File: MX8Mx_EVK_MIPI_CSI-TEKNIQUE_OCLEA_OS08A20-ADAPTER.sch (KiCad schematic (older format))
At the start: 11 parts, among them J1 1888863-4, J2 XF2M-3215-1A, U1 NLSX5014DTR2G, U2 SN74LVC1G14DRL

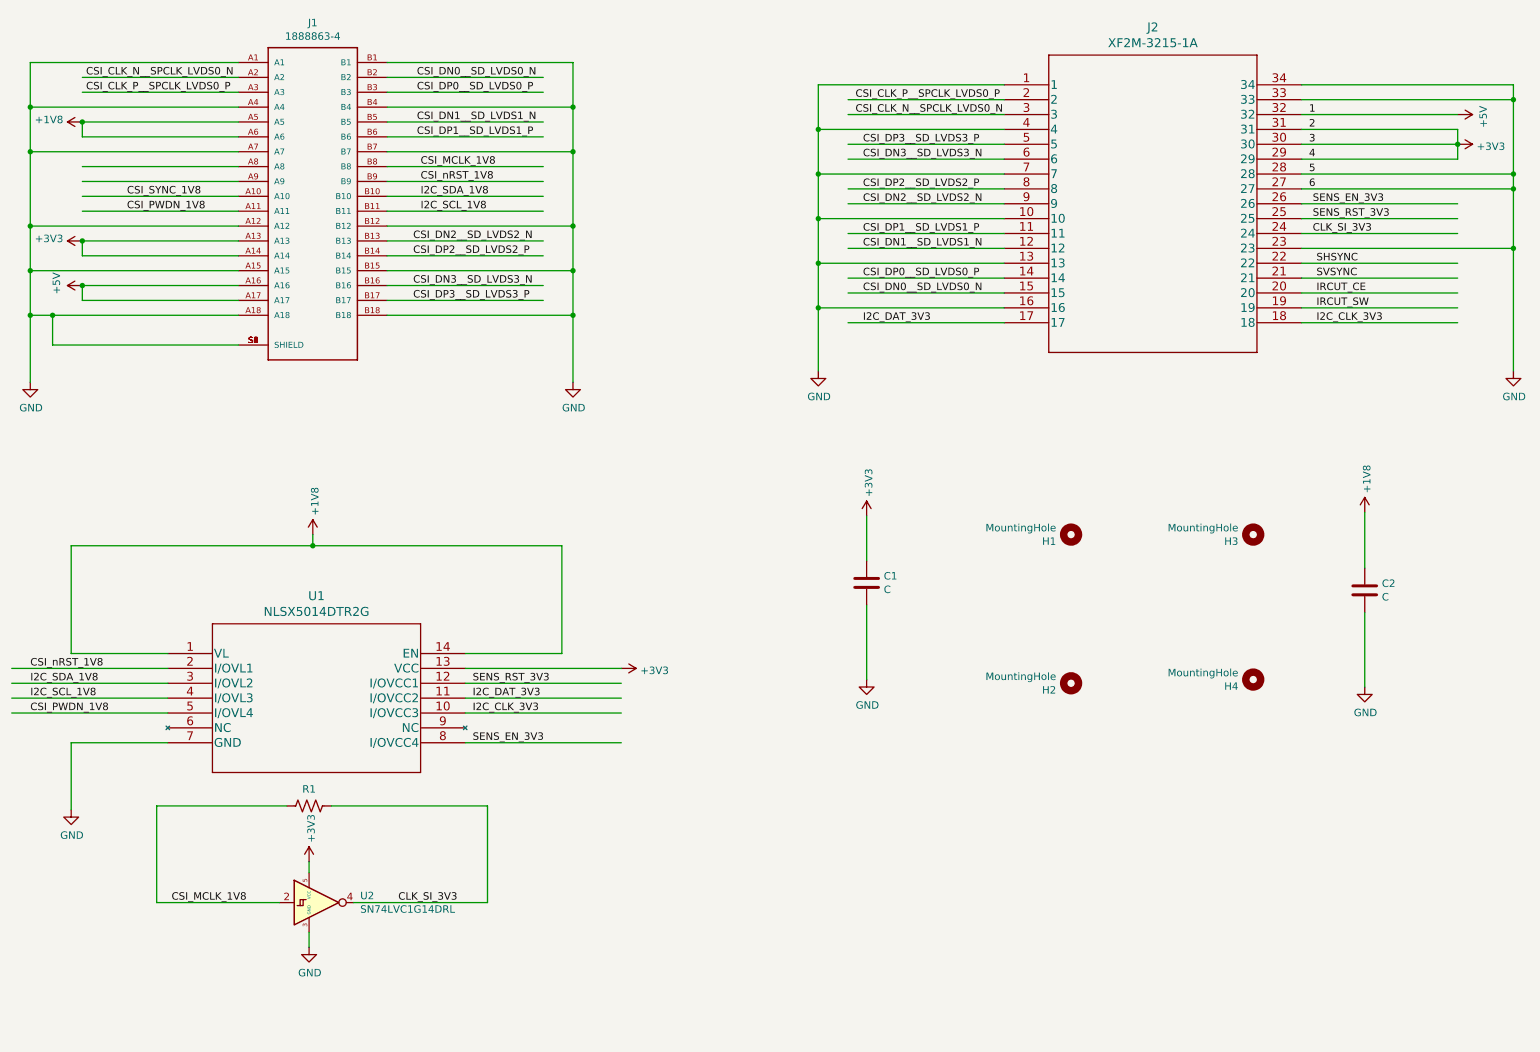
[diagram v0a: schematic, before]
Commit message: Mirror J1 signals (A-side to B-side and vice-versa) for mating with the MIPI-CSI interface(s) on EVK
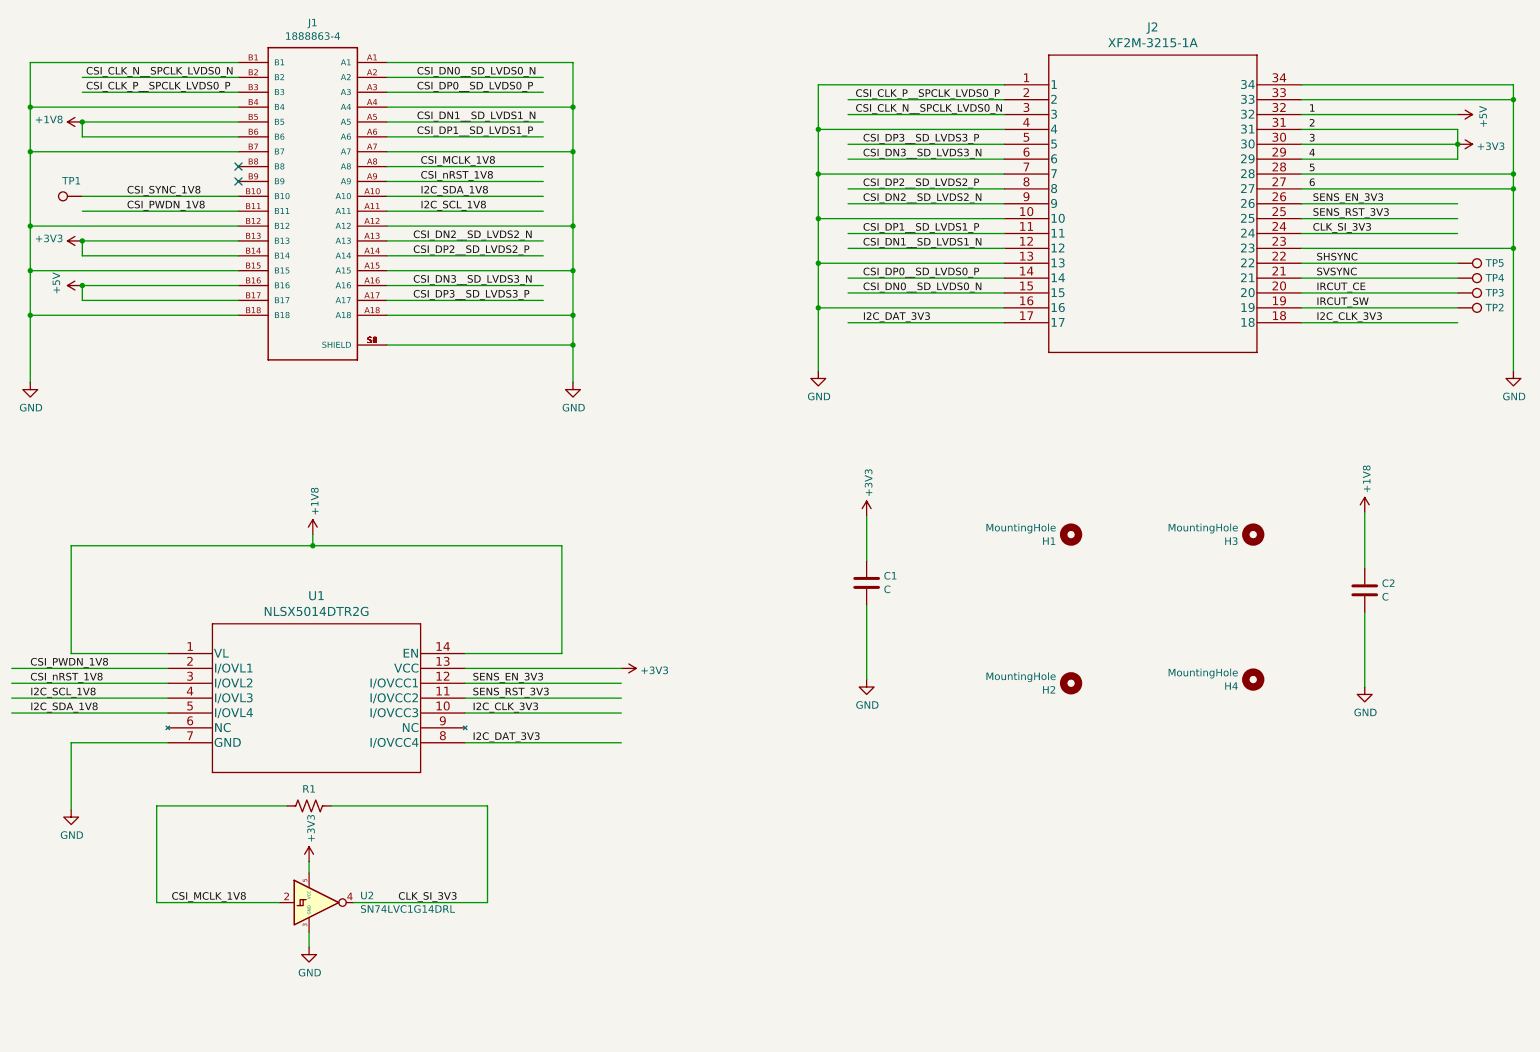
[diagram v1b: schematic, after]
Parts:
- added TP1, TP2, TP3, TP4, TP5: TestPoint, TestPoint:TestPoint_Pad_D1.0mm, symbol Connector:TestPoint
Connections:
- wire segments 131 -> 128
- no-connect marks 0 -> 2
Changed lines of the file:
@@
 	4300 1175 3250 1175
-Wire Wire Line
-	4300 1275 3250 1275
 Wire Wire Line
 	4300 1475 3250 1475
@@
 Text Label 3450 1175 0    50   ~ 0
 CSI_DN0__SD_LVDS0_N
-Text Label 3450 1275 0    50   ~ 0
-CSI_DP0__SD_LVDS0_P
 Text Label 3450 1475 0    50   ~ 0
 CSI_DN1__SD_LVDS1_N
@@
 	2750 4325 4425 4325
 Wire Wire Line
+	1775 5450 725  5450
+Wire Wire Line
+	1775 5350 725  5350
+Wire Wire Line
+	1775 5150 725  5150
+Wire Wire Line
 	1775 5250 725  5250
 Wire Wire Line
-	1775 5350 725  5350
-Wire Wire Line
-	1775 5450 725  5450
-Wire Wire Line
-	1775 5150 725  5150
+	4825 5650 3775 5650
+Wire Wire Line
+	4825 5450 3775 5450
+Wire Wire Line
+	4825 5250 3775 5250
 Wire Wire Line
 	4825 5350 3775 5350
-Wire Wire Line
-	4825 5450 3775 5450
-Wire Wire Line
-	4825 5650 3775 5650
-Wire Wire Line
-	4825 5250 3775 5250
-Wire Wire Line
-	3775 5150 4825 5150
 Wire Wire Line
 	1775 5650 1125 5650
@@
 Wire Wire Line
 	1125 4325 2750 4325
-Text Label 850  5250 0    50   ~ 0
+Text Label 850  5450 0    50   ~ 0
 I2C_SDA_1V8
 Text Label 850  5350 0    50   ~ 0
@@
 Text Label 3825 5450 0    50   ~ 0
 I2C_CLK_3V3
+Text Label 3825 5650 0    50   ~ 0
+I2C_DAT_3V3
+Text Label 850  5150 0    50   ~ 0
+CSI_PWDN_1V8
+Text Label 850  5250 0    50   ~ 0
+CSI_nRST_1V8
+Text Label 3825 5250 0    50   ~ 0
+SENS_EN_3V3
 Text Label 3825 5350 0    50   ~ 0
-I2C_DAT_3V3
-Text Label 850  5450 0    50   ~ 0
-CSI_PWDN_1V8
-Text Label 850  5150 0    50   ~ 0
-CSI_nRST_1V8
-Text Label 3825 5650 0    50   ~ 0
-SENS_EN_3V3
-Text Label 3825 5250 0    50   ~ 0
 SENS_RST_3V3
 $Comp
@@
 Wire Wire Line
 	3925 6075 3925 6725
-Wire Wire Line
-	2250 1775 1200 1775
-Wire Wire Line
-	2250 1875 1200 1875
 $Comp
 L Device:C C1
@@
 Wire Wire Line
 	9825 4100 9825 4475
-Wire Wire Line
-	1000 2775 850  2775
-Wire Wire Line
-	1000 2775 2250 2775
-Connection ~ 1000 2775
-Wire Wire Line
-	1000 2775 1000 2975
-Wire Wire Line
-	1000 2975 2250 2975
-Wire Wire Line
-	4500 2775 4500 3225
 $Comp
 L 1888863-4:1888863-4 J1
@@
 F 4 "Compliant" H 2750 2075 50  0001 L BNN "Field4"
 	1    2750 2075
-	1    0    0    -1
+	-1   0    0    -1
+$EndComp
+Wire Wire Line
+	850  2775 2250 2775
+Wire Wire Line
+	3250 2975 4500 2975
+Wire Wire Line
+	4500 2775 4500 2975
+Connection ~ 4500 2975
+Wire Wire Line
+	4500 2975 4500 3225
+Text Label 3450 1275 0    50   ~ 0
+CSI_DP0__SD_LVDS0_P
+Wire Wire Line
+	4300 1275 3250 1275
+Wire Wire Line
+	3775 5150 4825 5150
+$Comp
+L Connector:TestPoint TP1
+U 1 1 610FA21D
+P 1200 1975
+F 0 "TP1" V 1303 2047 50  0000 C CNN
+F 1 "TestPoint" V 1304 2047 50  0001 C CNN
+F 2 "TestPoint:TestPoint_Pad_D1.0mm" H 1400 1975 50  0001 C CNN
+F 3 "~" H 1400 1975 50  0001 C CNN
+	1    1200 1975
+	0    -1   -1   0
+$EndComp
+NoConn ~ 2250 1775
+NoConn ~ 2250 1875
+$Comp
+L Connector:TestPoint TP5
+U 1 1 6110F3C5
+P 10450 2425
+F 0 "TP5" V 10450 2613 50  0000 L CNN
+F 1 "TestPoint" V 10495 2613 50  0001 L CNN
+F 2 "TestPoint:TestPoint_Pad_D1.0mm" H 10650 2425 50  0001 C CNN
+F 3 "~" H 10650 2425 50  0001 C CNN
+	1    10450 2425
+	0    1    1    0
+$EndComp
+$Comp
+L Connector:TestPoint TP4
+U 1 1 6110ED4E
+P 10450 2525
+F 0 "TP4" V 10450 2713 50  0000 L CNN
+F 1 "TestPoint" V 10495 2713 50  0001 L CNN
+F 2 "TestPoint:TestPoint_Pad_D1.0mm" H 10650 2525 50  0001 C CNN
+F 3 "~" H 10650 2525 50  0001 C CNN
+	1    10450 2525
+	0    1    1    0
+$EndComp
+$Comp
+L Connector:TestPoint TP3
+U 1 1 6110E5F6
+P 10450 2625
+F 0 "TP3" V 10450 2813 50  0000 L CNN
+F 1 "TestPoint" V 10495 2813 50  0001 L CNN
+F 2 "TestPoint:TestPoint_Pad_D1.0mm" H 10650 2625 50  0001 C CNN
+F 3 "~" H 10650 2625 50  0001 C CNN
+	1    10450 2625
+	0    1    1    0
+$EndComp
+$Comp
+L Connector:TestPoint TP2
+U 1 1 6110DD9A
+P 10450 2725
+F 0 "TP2" V 10450 2913 50  0000 L CNN
+F 1 "TestPoint" V 10495 2913 50  0001 L CNN
+F 2 "TestPoint:TestPoint_Pad_D1.0mm" H 10650 2725 50  0001 C CNN
+F 3 "~" H 10650 2725 50  0001 C CNN
+	1    10450 2725
+	0    1    1    0
 $EndComp
 $EndSCHEMATC

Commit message: Change 32-pin connector from Omron XF2M-3215-1A to TE 3-1734592-2
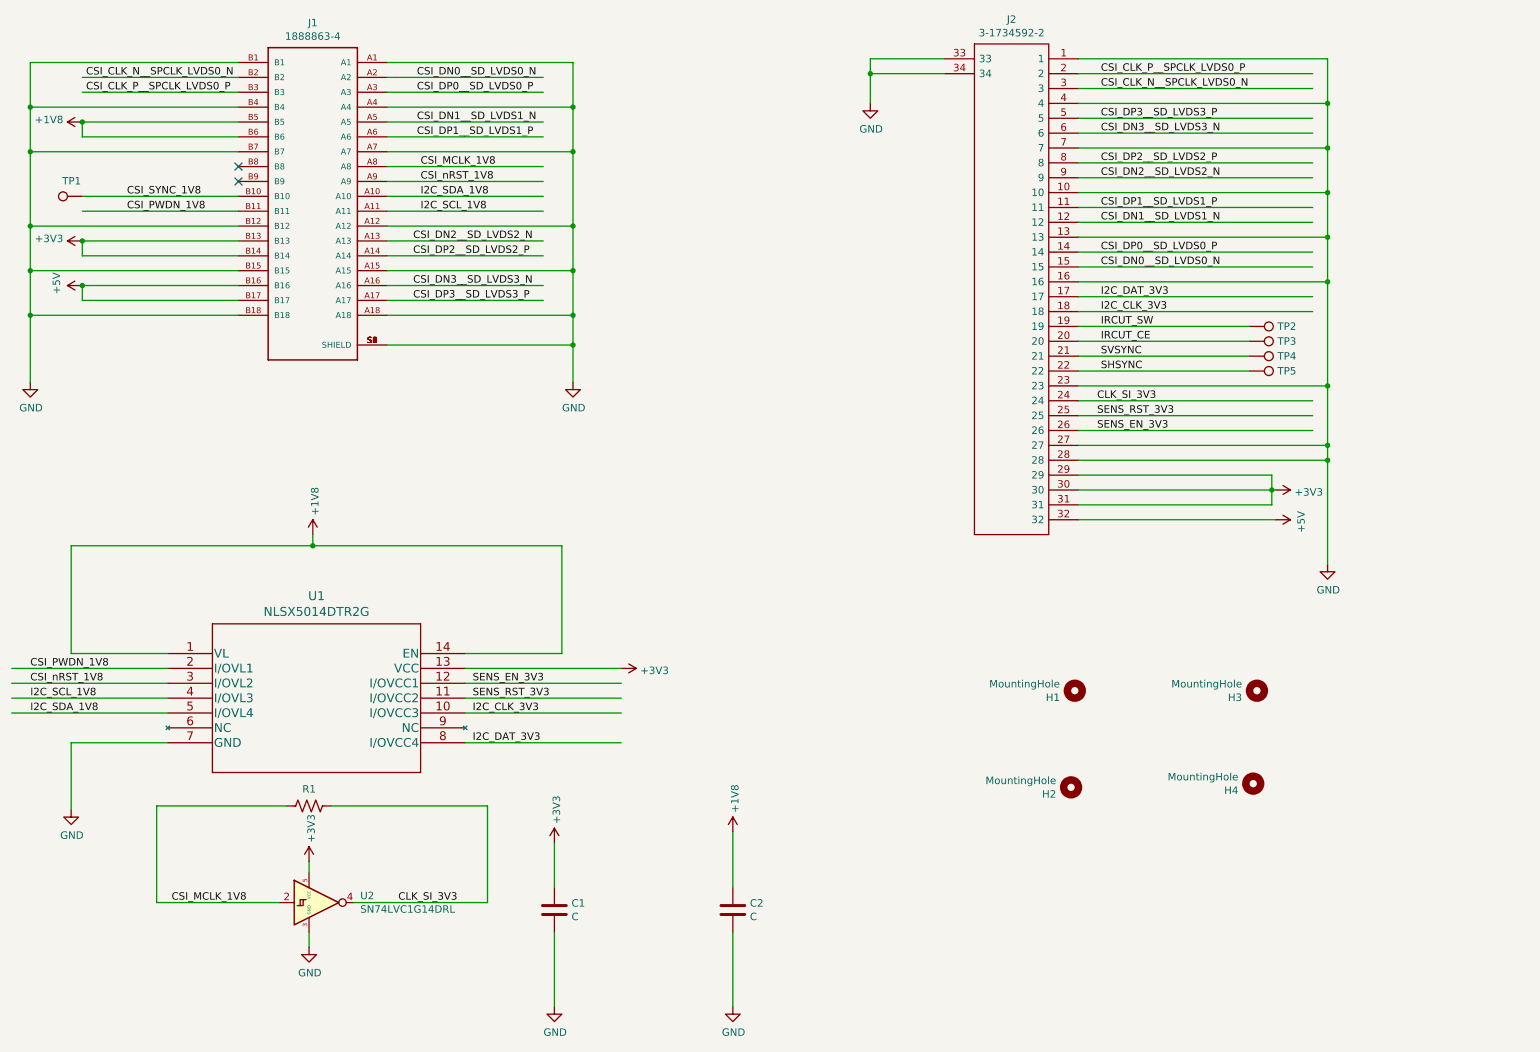
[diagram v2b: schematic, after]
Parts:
- removed J2: XF2M-3215-1A, footprints:XF2M-3215-1A, symbol XF2M-3215-1A:XF2M-3215-1A
- added J2: 3-1734592-2, footprints:317345922, symbol 3-1734592-2:3-1734592-2
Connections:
- net labels removed: 1, 2, 3, 4, 5, 6
- wire segments 128 -> 129
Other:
- moved on the sheet: C1, C2, H1, H2, H3, H4, TP2, TP3, TP4, TP5
